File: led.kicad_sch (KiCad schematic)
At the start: 384 parts, among them U1 IS31FL3729, U2 IS31FL3729, U3 IS31FL3729, U4 IS31FL3729

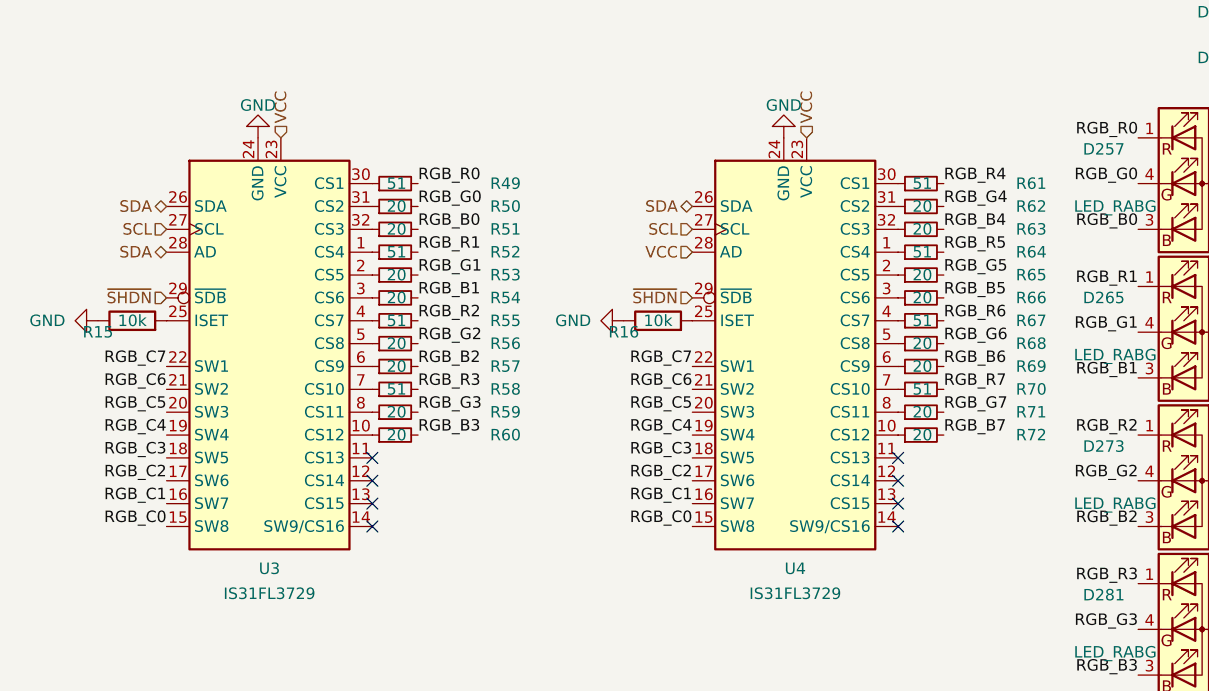
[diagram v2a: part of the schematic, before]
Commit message: routed PMU + rull RGB
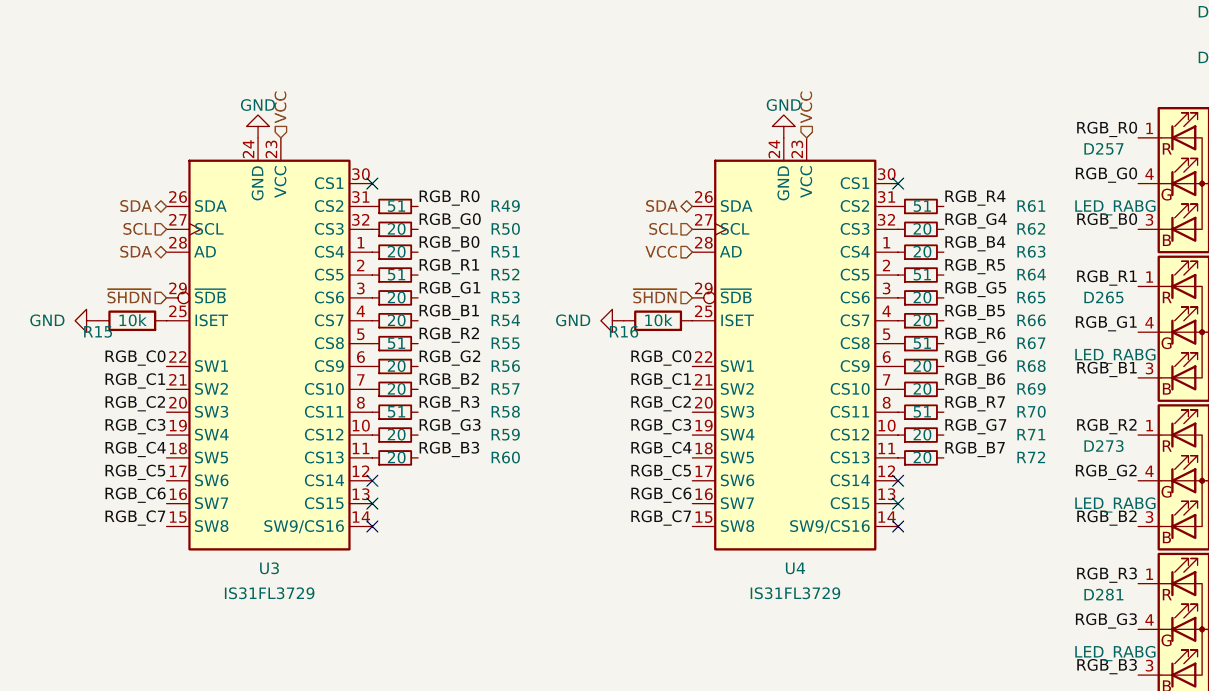
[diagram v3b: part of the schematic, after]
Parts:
- U1, U2, U3, U4: footprint Package_DFN_QFN:QFN-32-1EP_4x4mm_P0.4mm_EP2.9x2.9mm -> misc:eTQFP-32_7x7mm_P0.8mm
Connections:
- net RGB_C0: now also U3.22 (SW1), U4.22 (SW1); no longer U3.15 (SW8), U4.15 (SW8)
- net RGB_C1: now also U3.21 (SW2), U4.21 (SW2); no longer U3.16 (SW7), U4.16 (SW7)
- net RGB_C2: now also U3.20 (SW3), U4.20 (SW3); no longer U3.17 (SW6), U4.17 (SW6)
- net RGB_C3: now also U3.19 (SW4), U4.19 (SW4); no longer U3.18 (SW5), U4.18 (SW5)
- net RGB_C4: now also U3.18 (SW5), U4.18 (SW5); no longer U3.19 (SW4), U4.19 (SW4)
- net RGB_C5: now also U3.17 (SW6), U4.17 (SW6); no longer U3.20 (SW3), U4.20 (SW3)
- net RGB_C6: now also U3.16 (SW7), U4.16 (SW7); no longer U3.21 (SW2), U4.21 (SW2)
- net RGB_C7: now also U3.15 (SW8), U4.15 (SW8); no longer U3.22 (SW1), U4.22 (SW1)
- net at R72.1: now also U4.11 (CS13); no longer U4.10 (CS12)
- net at R59.1: now also U3.10 (CS12); no longer U3.8 (CS11)
- net at R52.1: now also U3.2 (CS5); no longer U3.1 (CS4)
- net at R60.1: now also U3.11 (CS13); no longer U3.10 (CS12)
- net at R67.1: now also U4.5 (CS8); no longer U4.4 (CS7)
- net at U4.1 (CS4): now also R63.1; no longer R64.1
- net at U4.2 (CS5): now also R64.1; no longer R65.1
- net at U4.3 (CS6): now also R65.1; no longer R66.1
- net at U4.30 (CS1): no longer R61.1
- net at U4.31 (CS2): now also R61.1; no longer R62.1
- net at U4.32 (CS3): now also R62.1; no longer R63.1
- net at R68.1: now also U4.6 (CS9); no longer U4.5 (CS8)
- net at R69.1: now also U4.7 (CS10); no longer U4.6 (CS9)
- net at R70.1: now also U4.8 (CS11); no longer U4.7 (CS10)
- net at R71.1: now also U4.10 (CS12); no longer U4.8 (CS11)
- net at R54.1: now also U3.4 (CS7); no longer U3.3 (CS6)
- net at R49.1: now also U3.31 (CS2); no longer U3.30 (CS1)
- net at R58.1: now also U3.8 (CS11); no longer U3.7 (CS10)
- net at R51.1: now also U3.1 (CS4); no longer U3.32 (CS3)
- net at R50.1: now also U3.32 (CS3); no longer U3.31 (CS2)
- net at R55.1: now also U3.5 (CS8); no longer U3.4 (CS7)
- net at R57.1: now also U3.7 (CS10); no longer U3.6 (CS9)
- net at R56.1: now also U3.6 (CS9); no longer U3.5 (CS8)
- net at R53.1: now also U3.3 (CS6); no longer U3.2 (CS5)
- new net: R66.1, U4.4 (CS7)
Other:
- moved on the sheet: R49, R50, R51, R52, R53, R54, R55, R56, R57, R58, R59, R60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

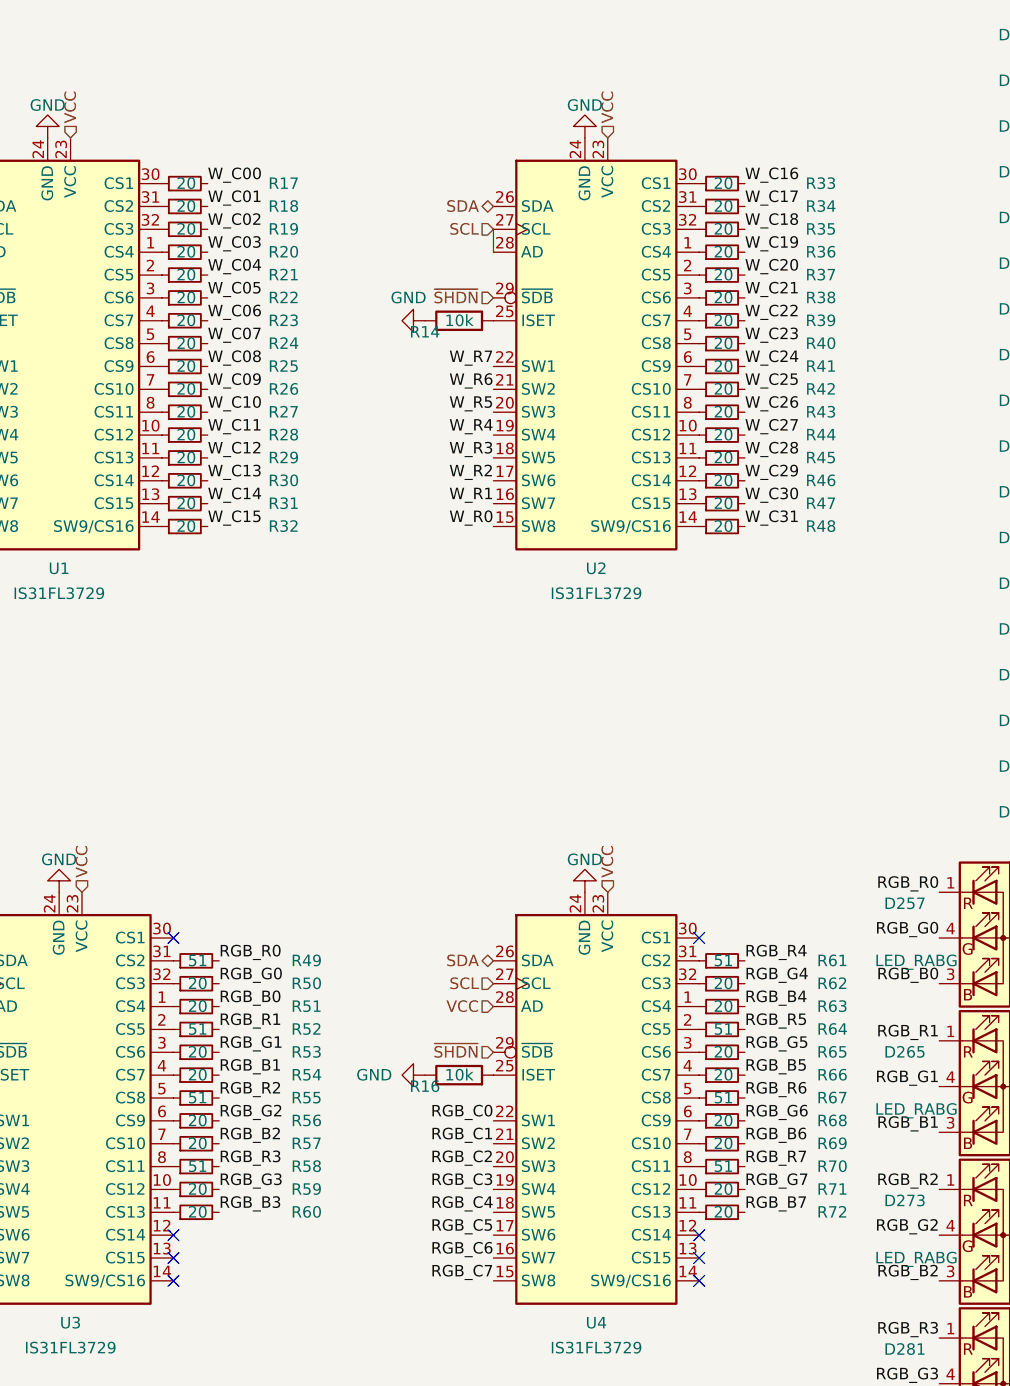
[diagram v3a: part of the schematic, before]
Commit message: rid of LED driver resistors
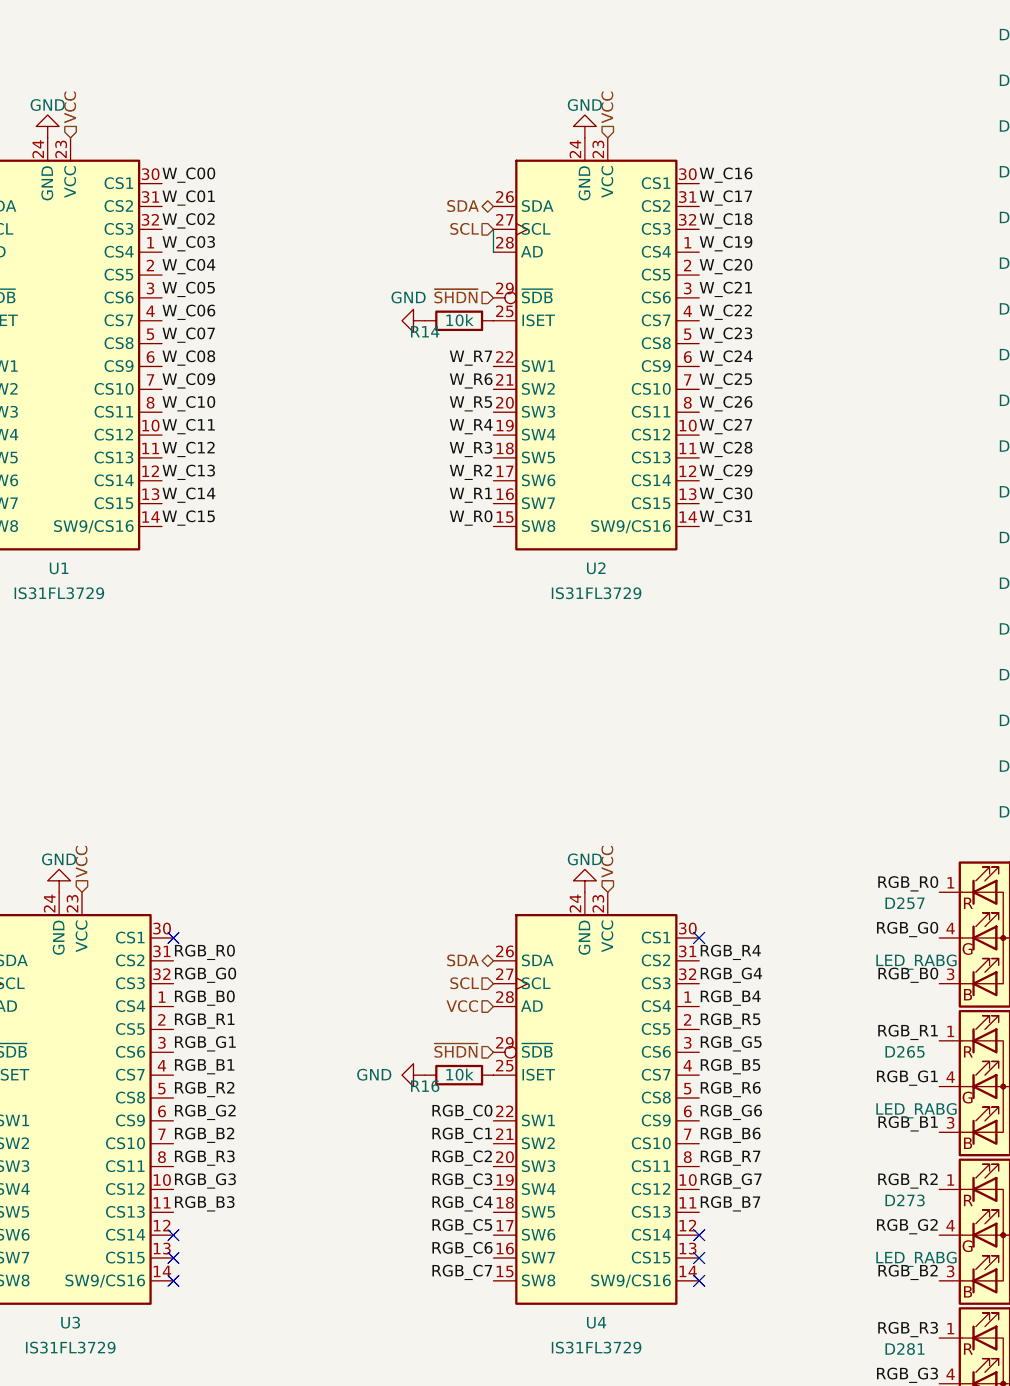
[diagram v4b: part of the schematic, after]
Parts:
- removed R17, R18, R19, R20, R21, R22, R23, R24, R25, R26, R27, R28, R29, R30, R31, R32, R33, R34, R35, R36, R37, R38, R39, R40, R41, R42, R43, R44, R45, R46, R47, R48, R50, R51, R53, R54, R56, R57, R59, R60, R62, R63, R65, R66, R68, R69, R71, R72: 20, Resistor_SMD:R_0603_1608Metric, symbol Device:R_Small
- removed R49, R52, R55, R58, R61, R64, R67, R70: 51, Resistor_SMD:R_0603_1608Metric, symbol Device:R_Small
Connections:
- net RGB_B0: now also U3.1 (CS4)
- net RGB_B1: now also U3.4 (CS7)
- net RGB_B2: now also U3.7 (CS10)
- net RGB_B3: now also U3.11 (CS13)
- net RGB_B4: now also U4.1 (CS4)
- net RGB_B5: now also U4.4 (CS7)
- net RGB_B6: now also U4.7 (CS10)
- net RGB_B7: now also U4.11 (CS13)
- net RGB_G0: now also U3.32 (CS3)
- net RGB_G1: now also U3.3 (CS6)
- net RGB_G2: now also U3.6 (CS9)
- net RGB_G3: now also U3.10 (CS12)
- net RGB_G4: now also U4.32 (CS3)
- net RGB_G5: now also U4.3 (CS6)
- net RGB_G6: now also U4.6 (CS9)
- net RGB_G7: now also U4.10 (CS12)
- net RGB_R0: now also U3.31 (CS2)
- net RGB_R1: now also U3.2 (CS5)
- net RGB_R2: now also U3.5 (CS8)
- net RGB_R3: now also U3.8 (CS11)
- net RGB_R4: now also U4.31 (CS2)
- net RGB_R5: now also U4.2 (CS5)
- net RGB_R6: now also U4.5 (CS8)
- net RGB_R7: now also U4.8 (CS11)
- net W_C00: now also U1.30 (CS1)
- net W_C01: now also U1.31 (CS2)
- net W_C02: now also U1.32 (CS3)
- net W_C03: now also U1.1 (CS4)
- net W_C04: now also U1.2 (CS5)
- net W_C05: now also U1.3 (CS6)
- net W_C06: now also U1.4 (CS7)
- net W_C07: now also U1.5 (CS8)
- net W_C08: now also U1.6 (CS9)
- net W_C09: now also U1.7 (CS10)
- net W_C10: now also U1.8 (CS11)
- net W_C11: now also U1.10 (CS12)
- net W_C12: now also U1.11 (CS13)
- net W_C13: now also U1.12 (CS14)
- net W_C14: now also U1.13 (CS15)
- net W_C15: now also U1.14 (SW9/CS16)
- net W_C16: now also U2.30 (CS1)
- net W_C17: now also U2.31 (CS2)
- net W_C18: now also U2.32 (CS3)
- net W_C19: now also U2.1 (CS4)
- net W_C20: now also U2.2 (CS5)
- net W_C21: now also U2.3 (CS6)
- net W_C22: now also U2.4 (CS7)
- net W_C23: now also U2.5 (CS8)
- net W_C24: now also U2.6 (CS9)
- net W_C25: now also U2.7 (CS10)
- net W_C26: now also U2.8 (CS11)
- net W_C27: now also U2.10 (CS12)
- net W_C28: now also U2.11 (CS13)
- net W_C29: now also U2.12 (CS14)
- net W_C30: now also U2.13 (CS15)
- net W_C31: now also U2.14 (SW9/CS16)

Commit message: first version
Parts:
- removed D257, D258, D259, D260, D261, D262, D263, D264, D265, D266, D267, D268, D269, D270, D271, D272, D273, D274, D275, D276, D277, D278, D279, D280, D281, D282, D283, D284, D285, D286, D287, D288, D289, D290, D291, D292, D293, D294, D295, D296, D297, D298, D299, D300, D301, D302, D303, D304, D305, D306, D307, D308, D309, D310, D311, D312, D313, D314, D315, D316, D317, D318, D319, D320: LED_RABG, LED_SMD:LED_ASMB-KTF0-0A306, symbol Device:LED_RABG
- added D257, D258, D259, D260, D261, D262, D263, D264, D265, D266, D267, D268, D269, D270, D271, D272, D273, D274, D275, D276, D277, D278, D279, D280, D281, D282, D283, D284, D285, D286, D287, D288, D289, D290, D291, D292, D293, D294, D295, D296, D297, D298, D299, D300, D301, D302, D303, D304, D305, D306, D307, D308, D309, D310, D311, D312, D313, D314, D315, D316, D317, D318, D319, D320: LED_BGRA, LED_SMD:LED_ASMB-KTF0-0A306, symbol Device:LED_BGRA
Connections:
- net RGB_B0: now also D257.1 (BK), D258.1 (BK), D259.1 (BK), D260.1 (BK), D261.1 (BK), D262.1 (BK), D263.1 (BK), D264.1 (BK)
- net RGB_B1: now also D265.1 (BK), D266.1 (BK), D267.1 (BK), D268.1 (BK), D269.1 (BK), D270.1 (BK), D271.1 (BK), D272.1 (BK)
- net RGB_B2: now also D273.1 (BK), D274.1 (BK), D275.1 (BK), D276.1 (BK), D277.1 (BK), D278.1 (BK), D279.1 (BK), D280.1 (BK)
- net RGB_B3: now also D281.1 (BK), D282.1 (BK), D283.1 (BK), D284.1 (BK), D285.1 (BK), D286.1 (BK), D287.1 (BK), D288.1 (BK)
- net RGB_B4: now also D289.1 (BK), D290.1 (BK), D291.1 (BK), D292.1 (BK), D293.1 (BK), D294.1 (BK), D295.1 (BK), D296.1 (BK)
- net RGB_B5: now also D297.1 (BK), D298.1 (BK), D299.1 (BK), D300.1 (BK), D301.1 (BK), D302.1 (BK), D303.1 (BK), D304.1 (BK)
- net RGB_B6: now also D305.1 (BK), D306.1 (BK), D307.1 (BK), D308.1 (BK), D309.1 (BK), D310.1 (BK), D311.1 (BK), D312.1 (BK)
- net RGB_B7: now also D313.1 (BK), D314.1 (BK), D315.1 (BK), D316.1 (BK), D317.1 (BK), D318.1 (BK), D319.1 (BK), D320.1 (BK)
- net RGB_C0: now also D257.4 (A), D265.4 (A), D273.4 (A), D281.4 (A), D289.4 (A), D297.4 (A), D305.4 (A), D313.4 (A)
- net RGB_C1: now also D258.4 (A), D266.4 (A), D274.4 (A), D282.4 (A), D290.4 (A), D298.4 (A), D306.4 (A), D314.4 (A)
- net RGB_C2: now also D259.4 (A), D267.4 (A), D275.4 (A), D283.4 (A), D291.4 (A), D299.4 (A), D307.4 (A), D315.4 (A)
- net RGB_C3: now also D260.4 (A), D268.4 (A), D276.4 (A), D284.4 (A), D292.4 (A), D300.4 (A), D308.4 (A), D316.4 (A)
- net RGB_C4: now also D261.4 (A), D269.4 (A), D277.4 (A), D285.4 (A), D293.4 (A), D301.4 (A), D309.4 (A), D317.4 (A)
- net RGB_C5: now also D262.4 (A), D270.4 (A), D278.4 (A), D286.4 (A), D294.4 (A), D302.4 (A), D310.4 (A), D318.4 (A)
- net RGB_C6: now also D263.4 (A), D271.4 (A), D279.4 (A), D287.4 (A), D295.4 (A), D303.4 (A), D311.4 (A), D319.4 (A)
- net RGB_C7: now also D264.4 (A), D272.4 (A), D280.4 (A), D288.4 (A), D296.4 (A), D304.4 (A), D312.4 (A), D320.4 (A)
- net RGB_G0: now also D257.2 (GK), D258.2 (GK), D259.2 (GK), D260.2 (GK), D261.2 (GK), D262.2 (GK), D263.2 (GK), D264.2 (GK)
- net RGB_G1: now also D265.2 (GK), D266.2 (GK), D267.2 (GK), D268.2 (GK), D269.2 (GK), D270.2 (GK), D271.2 (GK), D272.2 (GK)
- net RGB_G2: now also D273.2 (GK), D274.2 (GK), D275.2 (GK), D276.2 (GK), D277.2 (GK), D278.2 (GK), D279.2 (GK), D280.2 (GK)
- net RGB_G3: now also D281.2 (GK), D282.2 (GK), D283.2 (GK), D284.2 (GK), D285.2 (GK), D286.2 (GK), D287.2 (GK), D288.2 (GK)
- net RGB_G4: now also D289.2 (GK), D290.2 (GK), D291.2 (GK), D292.2 (GK), D293.2 (GK), D294.2 (GK), D295.2 (GK), D296.2 (GK)
- net RGB_G5: now also D297.2 (GK), D298.2 (GK), D299.2 (GK), D300.2 (GK), D301.2 (GK), D302.2 (GK), D303.2 (GK), D304.2 (GK)
- net RGB_G6: now also D305.2 (GK), D306.2 (GK), D307.2 (GK), D308.2 (GK), D309.2 (GK), D310.2 (GK), D311.2 (GK), D312.2 (GK)
- net RGB_G7: now also D313.2 (GK), D314.2 (GK), D315.2 (GK), D316.2 (GK), D317.2 (GK), D318.2 (GK), D319.2 (GK), D320.2 (GK)
- net RGB_R0: now also D257.3 (RK), D258.3 (RK), D259.3 (RK), D260.3 (RK), D261.3 (RK), D262.3 (RK), D263.3 (RK), D264.3 (RK)
- net RGB_R1: now also D265.3 (RK), D266.3 (RK), D267.3 (RK), D268.3 (RK), D269.3 (RK), D270.3 (RK), D271.3 (RK), D272.3 (RK)
- net RGB_R2: now also D273.3 (RK), D274.3 (RK), D275.3 (RK), D276.3 (RK), D277.3 (RK), D278.3 (RK), D279.3 (RK), D280.3 (RK)
- net RGB_R3: now also D281.3 (RK), D282.3 (RK), D283.3 (RK), D284.3 (RK), D285.3 (RK), D286.3 (RK), D287.3 (RK), D288.3 (RK)
- net RGB_R4: now also D289.3 (RK), D290.3 (RK), D291.3 (RK), D292.3 (RK), D293.3 (RK), D294.3 (RK), D295.3 (RK), D296.3 (RK)
- net RGB_R5: now also D297.3 (RK), D298.3 (RK), D299.3 (RK), D300.3 (RK), D301.3 (RK), D302.3 (RK), D303.3 (RK), D304.3 (RK)
- net RGB_R6: now also D305.3 (RK), D306.3 (RK), D307.3 (RK), D308.3 (RK), D309.3 (RK), D310.3 (RK), D311.3 (RK), D312.3 (RK)
- net RGB_R7: now also D313.3 (RK), D314.3 (RK), D315.3 (RK), D316.3 (RK), D317.3 (RK), D318.3 (RK), D319.3 (RK), D320.3 (RK)
